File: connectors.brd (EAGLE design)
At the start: 14.5 x 14.5 mm, 19 parts, among them CON1 CON-4P-JST_GH-RA, CON2 CON-4P-JST_GH-RA, CON20 PINHEAD_1X03-2.54-RA, CON4 PINHEAD_1X02-2, CON5 PINHEAD_1X02-2, CON6 PINHEAD_1X07-2, IC1 TJA1051, IC2 TPD3S014DBVR-SOT23-6

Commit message: Library update
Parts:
- CON1, CON2: value CON-4P-JST_GH-RA -> CON-4P-TABS-JST_GH-RA
- flipped CON1 to the top
- flipped CON2 to the bottom
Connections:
- net N$23 renamed CANH
- net N$35 renamed CANL
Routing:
- net CAN1_VDD: track 11.2 -> 11.9 mm, vias 3 -> 4

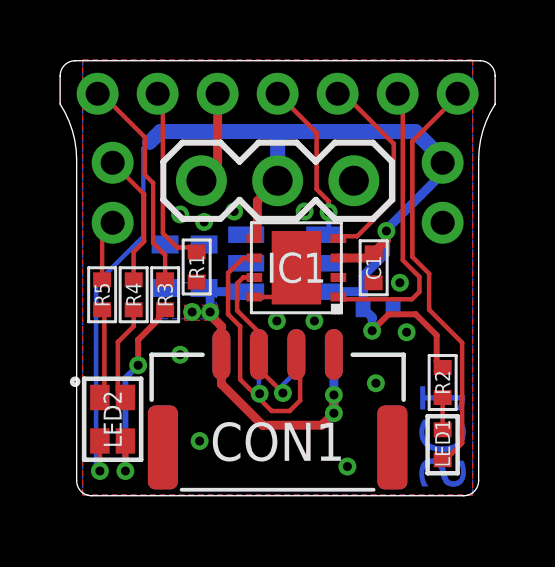
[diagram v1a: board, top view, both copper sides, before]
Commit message: Change R1 to 27K (#17)
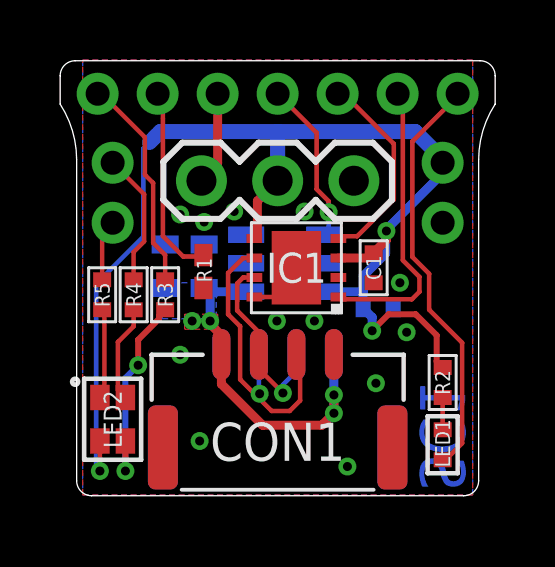
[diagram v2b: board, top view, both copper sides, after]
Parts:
- R1: value 1K -> 27K; device R_digikey:R0402 -> RC0402FR-0727KL:RESC1005X40N
- moved R1 0.27 mm to (-2.48, 4.97), turned to 270 degrees
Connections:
- net ADJ: now also R1.1; no longer R1.2
- net GND: now also R1.2; no longer R1.1
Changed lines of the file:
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@@
 <?xml version="1.0" encoding="utf-8"?>
 <!DOCTYPE eagle SYSTEM "eagle.dtd">
-<eagle version="9.3.2">
+<eagle version="9.6.2">
 <drawing>
 <settings>
@@
 <setting verticaltext="up"/>
 </settings>
-<grid distance="0.025" unitdist="mm" unit="mm" style="lines" multiple="1" display="no" altdistance="5" altunitdist="mil" altunit="mil"/>
+<grid distance="0.1" unitdist="mm" unit="mm" style="lines" multiple="1" display="yes" altdistance="0.01" altunitdist="mm" altunit="mm"/>
 <layers>
 <layer number="1" name="Top" color="4" fill="1" visible="yes" active="yes"/>
@@
 </layers>
 <board>
-<fusionsync huburn="a.cGVyc29uYWw6dWUyYWE4ZDY4" projecturn="a.cGVyc29uYWw6dWUyYWE4ZDY4IzIwMTgxMTA4MTU5MTUwNTA2" f3durn="urn:adsk.wipprod:dm.lineage:ZQS02HFHRVyiMdq_vKv9Iw" pcbguid="7353c2ad-46a7-4ea5-9c06-792c71bb0b67" lastpulledtime="" lastsyncedchangeguid="f716055f-b493-9ca3-6809-f24e8c82e96c"/>
+<fusionsync huburn="a.cGVyc29uYWw6dWUyYWE4ZDY4" projecturn="a.cGVyc29uYWw6dWUyYWE4ZDY4IzIwMTgxMTA4MTU5MTUwNTA2" f3durn="urn:adsk.wipprod:dm.lineage:ZQS02HFHRVyiMdq_vKv9Iw" pcbguid="7353c2ad-46a7-4ea5-9c06-792c71bb0b67" lastpulledtime="" lastsyncedchangeguid="f716055f-b493-9ca3-6809-f24e8c82e96c" latestrevisionid="" lastsyncedrevisionid="" lastboardhashguid="" lastpushedtime="" linktopcb3d="false"/>
 <plain>
 <wire x1="-20" y1="0" x2="0" y2="20" width="0.01" layer="48" curve="-90"/>
@@
 <attribute name="MANF#" value="0022286030" x="0" y="8" size="1.778" layer="27" rot="R180" display="off"/>
 </element>
-<element name="R1" library="R_digikey" library_urn="urn:adsk.eagle:library:2539499" package="R0402" package3d_urn="urn:adsk.eagle:package:2539512/2" value="1K" x="-2.7" y="5.125" smashed="yes" rot="R90">
-<attribute name="DIGIKEY#" value="311-1.00KLRCT-ND" x="-2.7" y="5.125" size="1.778" layer="27" rot="R90" display="off"/>
-<attribute name="MANF" value="Yageo" x="-2.7" y="5.125" size="1.778" layer="27" rot="R90" display="off"/>
-<attribute name="MANF#" value="RC0402FR-071KL" x="-2.7" y="5.125" size="1.778" layer="27" rot="R90" display="off"/>
-<attribute name="NAME" x="-2.7" y="5.125" size="0.5" layer="25" font="vector" ratio="15" rot="R90" align="center"/>
-<attribute name="PACKAGE" value="0402" x="-2.7" y="5.125" size="1.778" layer="27" rot="R90" display="off"/>
-<attribute name="TOLERANCE" value="1%" x="-2.7" y="5.125" size="1.778" layer="27" rot="R90" display="off"/>
-<attribute name="VALUE" x="-3.6" y="5.125" size="0.5" layer="27" font="vector" ratio="15" rot="R90" align="center"/>
-</element>
 <element name="IC2" library="myxa_masterlib" library_urn="urn:adsk.eagle:library:1040030" package="SOT26" package3d_urn="urn:adsk.eagle:package:1040217/3" value="TPD3S014DBVR-SOT23-6" x="0.25" y="5.25" smashed="yes" rot="MR0">
 <attribute name="DIGIKEY#" value="296-38835-1-ND" x="0.25" y="5.25" size="1.778" layer="28" rot="MR0" display="off"/>
@@
 <attribute name="MANF#" value="SM04B-GHS-TB(LF)(SN)" x="0" y="-0.7" size="1.778" layer="28" rot="MR180" display="off"/>
 <attribute name="NAME" x="0" y="-0.7" size="1.27" layer="26" font="vector" ratio="15" rot="MR180" align="center"/>
+</element>
+<element name="R1" library="RC0402FR-0727KL" package="RESC1005X40N" value="27K" x="-2.475" y="4.975" smashed="yes" rot="R270">
+<attribute name="DESCRIPTION" value="YAGEO - AF0402FR-0727KL - SMD Chip Resistor, 27 kohm, +/- 1%, 62.5 mW, 0402 [1005 Metric], Thick Film, General Purpose" x="-2.475" y="4.975" size="1.778" layer="27" rot="R270" display="off"/>
+<attribute name="HEIGHT" value="0.32mm" x="-2.475" y="4.975" size="1.778" layer="27" rot="R270" display="off"/>
+<attribute name="MANUFACTURER_NAME" value="YAGEO" x="-2.475" y="4.975" size="1.778" layer="27" rot="R270" display="off"/>
+<attribute name="MANUFACTURER_PART_NUMBER" value="AF0402FR-0727KL" x="-2.475" y="4.975" size="1.778" layer="27" rot="R270" display="off"/>
+<attribute name="MOUSER_PART_NUMBER" value="" x="-2.475" y="4.975" size="1.778" layer="27" rot="R270" display="off"/>
+<attribute name="MOUSER_PRICE-STOCK" value="" x="-2.475" y="4.975" size="1.778" layer="27" rot="R270" display="off"/>
+<attribute name="NAME" x="-2.45" y="5.025" size="0.5" layer="25" rot="R270" align="center"/>
+<attribute name="PACKAGE" value="0402" x="-2.475" y="4.975" size="1.778" layer="27" rot="R270" display="off"/>
+<attribute name="VALUE" x="-2.475" y="4.975" size="1.27" layer="27" rot="R270" align="center"/>
 </element>
 </elements>
@@
 <contactref element="CON20" pad="1"/>
 <contactref element="CON5" pad="1"/>
-<contactref element="R1" pad="1"/>
 <via x="4.075" y="4.6" extent="1-16" drill="0.3" diameter="0.6"/>
 <via x="-2.6" y="-0.675" extent="1-16" drill="0.3" diameter="0.6"/>
@@
 <contactref element="CON2" pad="M$0"/>
 <contactref element="CON2" pad="M$1"/>
+<contactref element="R1" pad="2"/>
+<wire x1="0.9" y1="6.975" x2="2.54" y2="8" width="0" layer="19" extent="1-1"/>
+<wire x1="1.55" y1="5.25" x2="0.9" y2="6.975" width="0" layer="19" extent="16-16"/>
+<wire x1="2.025" y1="4.775" x2="1.55" y2="5.25" width="0" layer="19" extent="1-16"/>
+<wire x1="0.625" y1="5.1" x2="1.55" y2="5.25" width="0" layer="19" extent="1-16"/>
+<wire x1="0.6625" y1="4.85" x2="0.625" y2="5.1" width="0" layer="19" extent="1-1"/>
+<wire x1="-0.025" y1="3.325" x2="-0.775" y2="4.125" width="0" layer="19" extent="1-1"/>
+<wire x1="3.2" y1="4.6" x2="2.025" y2="4.775" width="0" layer="19" extent="1-1"/>
+<wire x1="4.075" y1="4.6" x2="3.2" y2="4.6" width="0" layer="19" extent="1-1"/>
+<wire x1="3.85" y1="3.75" x2="4.075" y2="4.6" width="0" layer="19" extent="16-16"/>
+<wire x1="4.3" y1="2.95" x2="3.85" y2="3.75" width="0" layer="19" extent="16-16"/>
+<wire x1="1.225" y1="3.325" x2="-0.025" y2="3.325" width="0" layer="19" extent="1-1"/>
+<wire x1="1.875" y1="2.21" x2="1.225" y2="3.325" width="0" layer="19" extent="1-1"/>
+<wire x1="3.275" y1="1.25" x2="1.875" y2="2.21" width="0" layer="19" extent="1-1"/>
+<wire x1="-1.875" y1="2.21" x2="-0.025" y2="3.325" width="0" layer="19" extent="16-16"/>
+<wire x1="-3.25" y1="2.2" x2="-1.875" y2="2.21" width="0" layer="19" extent="16-16"/>
+<wire x1="3.825" y1="-0.89" x2="3.275" y2="1.25" width="0" layer="19" extent="1-1"/>
+<wire x1="3.825" y1="-0.89" x2="3.825" y2="-0.89" width="0" layer="19" extent="1-16"/>
+<wire x1="2.325" y1="-1.525" x2="3.825" y2="-0.89" width="0" layer="19" extent="1-1"/>
+<wire x1="-2.475" y1="4.425" x2="-0.775" y2="4.125" width="0" layer="19" extent="1-1"/>
+<wire x1="-2.45" y1="5.875" x2="-2.475" y2="4.425" width="0" layer="19" extent="1-16"/>
+<wire x1="-2.45" y1="6.625" x2="-2.45" y2="5.875" width="0" layer="19" extent="16-16"/>
+<wire x1="-3.25" y1="6.875" x2="-2.45" y2="6.625" width="0" layer="19" extent="1-1"/>
+<wire x1="-1.45" y1="6.975" x2="-2.45" y2="6.625" width="0" layer="19" extent="1-1"/>
+<wire x1="-3.75" y1="5.875" x2="-3.25" y2="6.875" width="0" layer="19" extent="16-16"/>
+<wire x1="5.5" y1="6.6" x2="4.075" y2="4.6" width="0" layer="19" extent="1-1"/>
+<wire x1="-2.6" y1="-0.675" x2="-3.25" y2="2.2" width="0" layer="19" extent="1-1"/>
+<wire x1="-3.825" y1="-0.89" x2="-2.6" y2="-0.675" width="0" layer="19" extent="1-1"/>
+<wire x1="-3.825" y1="-0.89" x2="-3.825" y2="-0.89" width="0" layer="19" extent="1-16"/>
 </signal>
 <signal name="CAN1_TX">
@@
 </signal>
 <signal name="ADJ">
-<contactref element="R1" pad="2"/>
-<wire x1="-2.7" y1="5.625" x2="-2.85" y2="5.775" width="0.1524" layer="1"/>
-<wire x1="-2.85" y1="5.775" x2="-3.35" y2="5.775" width="0.1524" layer="1"/>
-<wire x1="-3.35" y1="5.775" x2="-3.825" y2="6.25" width="0.1524" layer="1"/>
-<wire x1="-3.825" y1="10.075" x2="-3.825" y2="6.25" width="0.1524" layer="1"/>
+<wire x1="-2.45" y1="5.475" x2="-3.15" y2="5.475" width="0.1524" layer="1"/>
+<wire x1="-3.15" y1="5.475" x2="-3.825" y2="6.15" width="0.1524" layer="1"/>
+<wire x1="-3.825" y1="10.075" x2="-3.825" y2="6.15" width="0.1524" layer="1"/>
 <contactref element="CON6" pad="6"/>
 <wire x1="-4" y1="10.9" x2="-3.825" y2="10.725" width="0.15" layer="1"/>
 <wire x1="-3.825" y1="10.725" x2="-3.825" y2="10.075" width="0.15" layer="1"/>
+<contactref element="R1" pad="1"/>
+<wire x1="-2.475" y1="5.525" x2="-2.45" y2="5.475" width="0" layer="19" extent="1-1"/>
 </signal>
 <signal name="CAN1_VDD">
@@
 <wire x1="-2.325" y1="4.3" x2="-2.45" y2="4.425" width="0.3" layer="16"/>
 <wire x1="-2.45" y1="4.425" x2="-2.25" y2="4.225" width="0.3" layer="16"/>
-<wire x1="-2.25" y1="4.225" x2="-2.25" y2="3.625" width="0.3" layer="16"/>
-<via x="-2.25" y="3.625" extent="1-16" drill="0.3" diameter="0.6"/>
-<wire x1="-2.25" y1="3.625" x2="-2.25" y2="3.525" width="0.3" layer="1"/>
-<wire x1="-2.25" y1="3.525" x2="-1.875" y2="3.15" width="0.3" layer="1"/>
-<via x="-2.85" y="3.625" extent="1-16" drill="0.3" diameter="0.6"/>
+<wire x1="-2.25" y1="4.225" x2="-2.25" y2="3.325" width="0.3" layer="16"/>
+<via x="-2.25" y="3.325" extent="1-16" drill="0.3" diameter="0.6"/>
+<wire x1="-2.25" y1="3.325" x2="-2.25" y2="3.225" width="0.3" layer="1"/>
+<wire x1="-2.25" y1="3.225" x2="-1.875" y2="2.85" width="0.3" layer="1"/>
+<via x="-2.85" y="3.325" extent="1-16" drill="0.3" diameter="0.6"/>
 <polygon width="0.2" layer="16" thermals="no">
 <vertex x="-3.85" y="4.6"/>
@@
 </polygon>
 <polygon width="0.2" layer="1" thermals="no">
-<vertex x="-2" y="3.85"/>
-<vertex x="-3.1" y="3.85"/>
-<vertex x="-3.1" y="3.35"/>
-<vertex x="-2" y="3.35"/>
+<vertex x="-2" y="3.55"/>
+<vertex x="-3.1" y="3.55"/>
+<vertex x="-3.1" y="3.05"/>
+<vertex x="-2" y="3.05"/>
 </polygon>
 <contactref element="CON1" pad="1"/>
 <contactref element="CON2" pad="1"/>
-<wire x1="-1.875" y1="3.15" x2="-1.875" y2="2.21" width="0.3" layer="1"/>
+<wire x1="-1.875" y1="2.85" x2="-1.875" y2="2.21" width="0.3" layer="1"/>
 <wire x1="-1.875" y1="2.21" x2="-1.875" y2="1.225" width="0.3" layer="1"/>
 <wire x1="-1.875" y1="1.225" x2="-0.5" y2="-0.15" width="0.3" layer="1"/>
